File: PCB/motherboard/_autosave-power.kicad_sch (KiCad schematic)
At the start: 28 parts, among them U1 TPS54140ADGQR, U2 PTPS259830LNRGER, U3 AP2112K-3.3TRG1

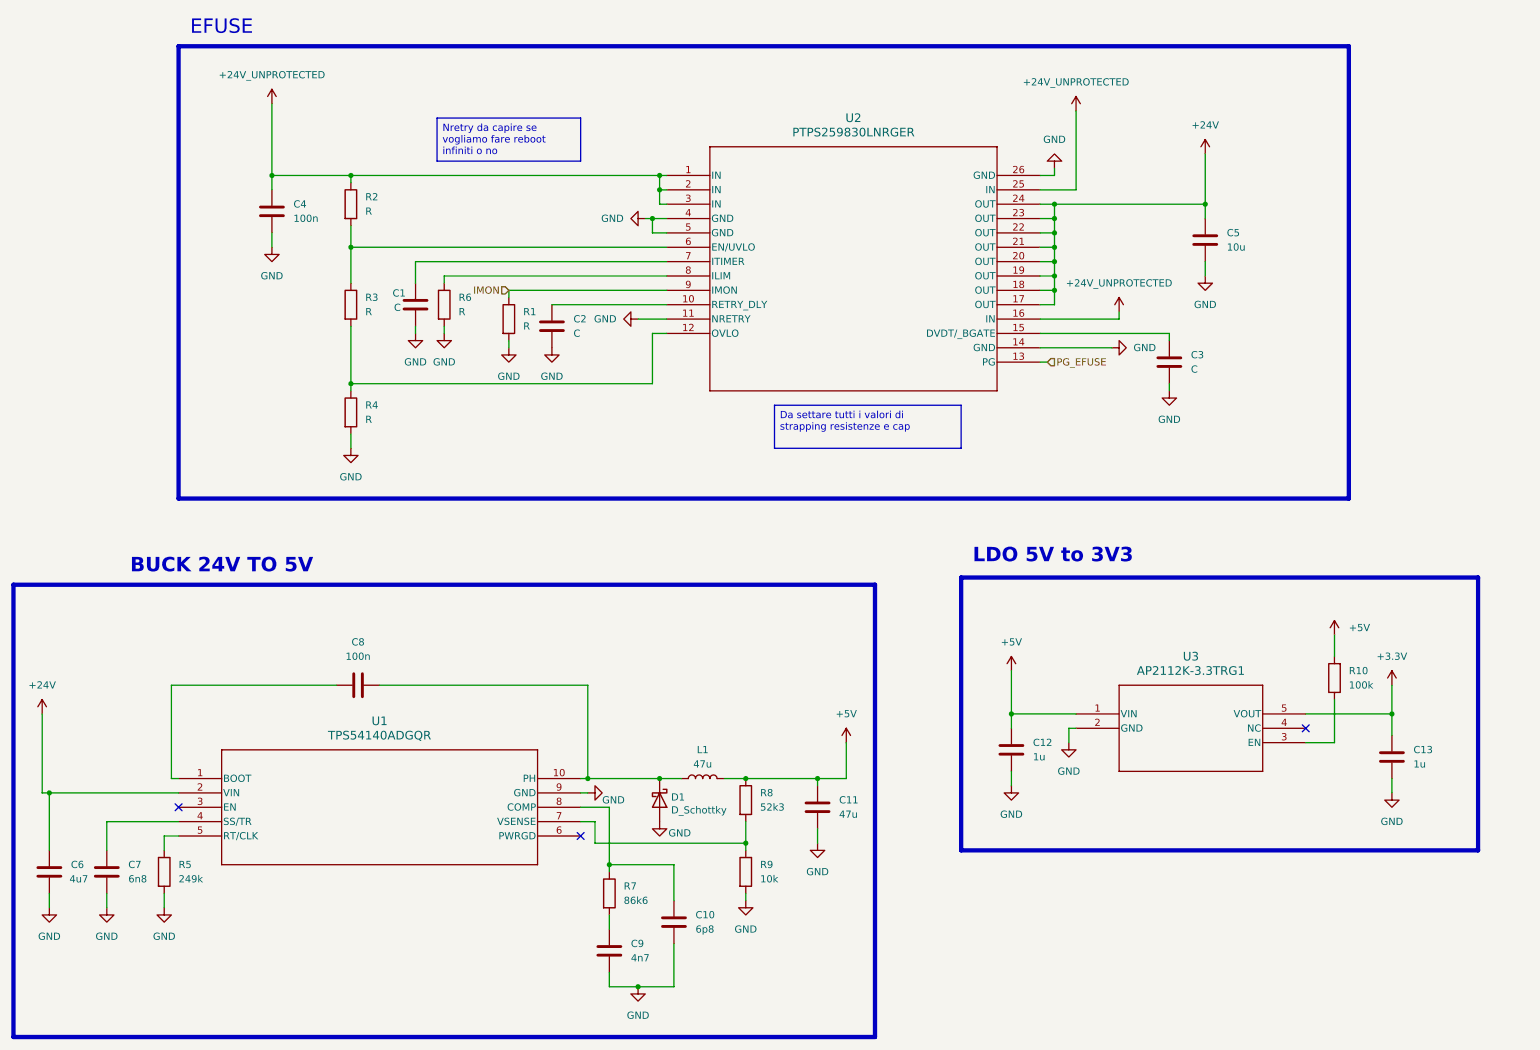
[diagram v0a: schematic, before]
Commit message: aggiunto driver escon in libreria e nel progetto schematico
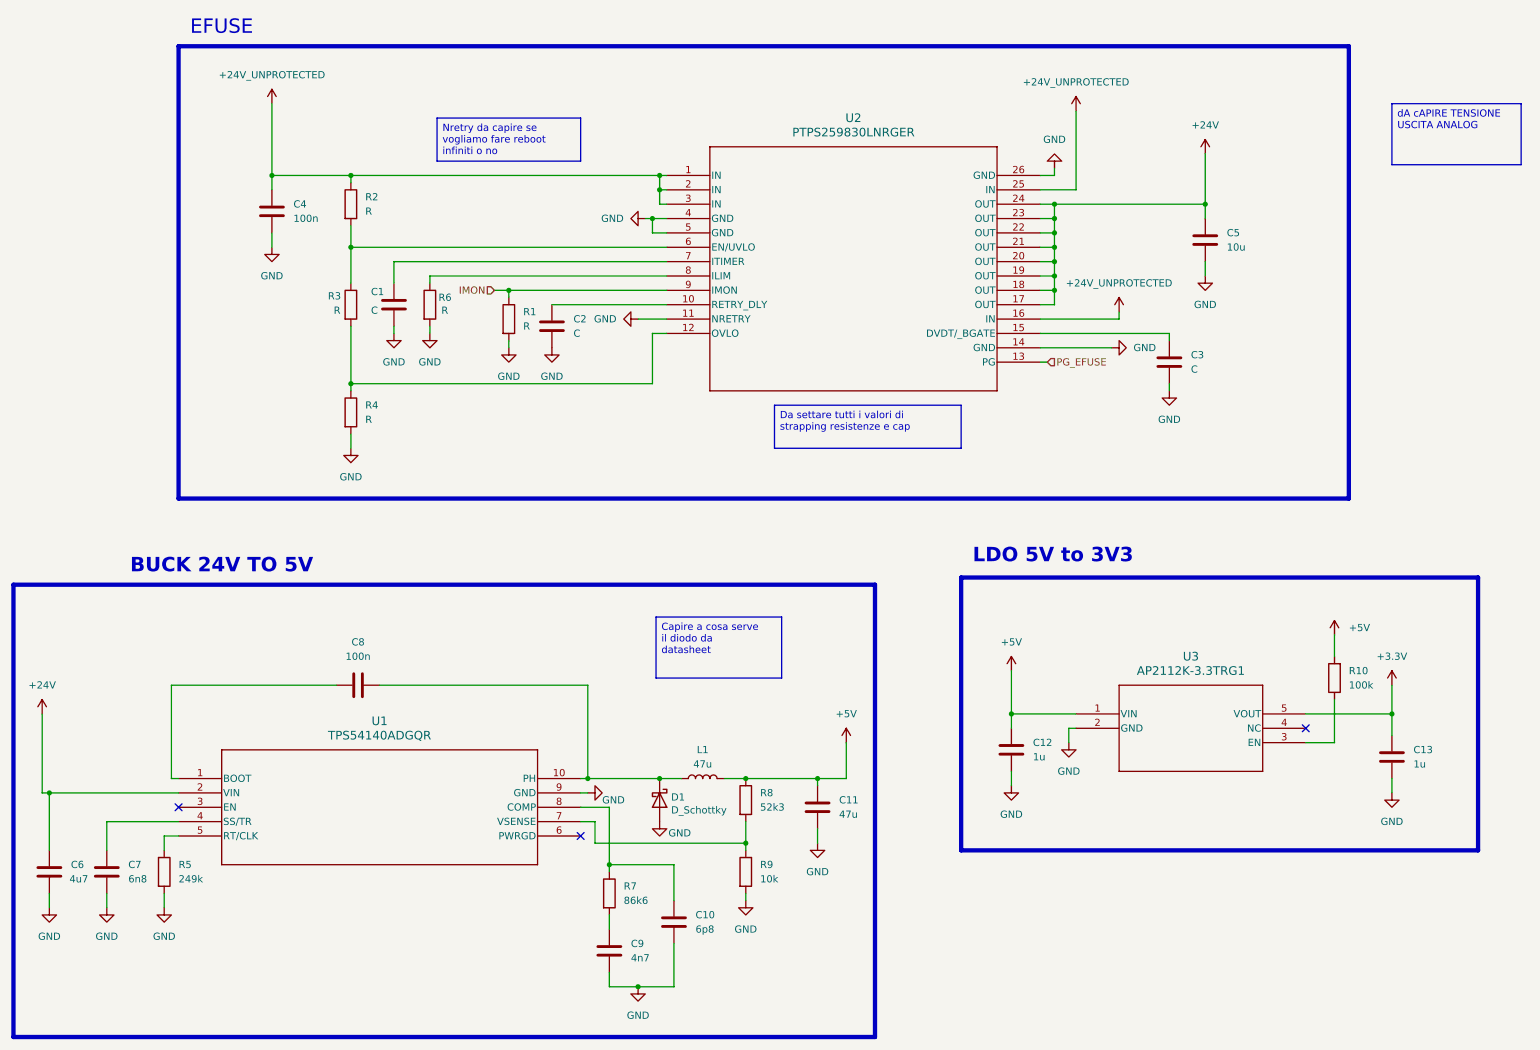
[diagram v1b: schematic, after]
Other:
- moved on the sheet: C1, R6
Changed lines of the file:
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@@
 		)
 	)
+	(text_box "dA cAPIRE TENSIONE USCITA ANALOG \n"
+		(exclude_from_sim no)
+		(at 260.35 27.94 0)
+		(size 22.86 10.795)
+		(margins 0.9525 0.9525 0.9525 0.9525)
+		(stroke
+			(width 0)
+			(type solid)
+		)
+		(fill
+			(type none)
+		)
+		(effects
+			(font
+				(size 1.27 1.27)
+			)
+			(justify left top)
+		)
+	)
 	(text_box "Da settare tutti i valori di strapping resistenze e cap\n"
 		(exclude_from_sim no)
@@
 		)
 	)
+	(text_box "Capire a cosa serve il diodo da datasheet"
+		(exclude_from_sim no)
+		(at 130.175 118.745 0)
+		(size 22.225 10.795)
+		(margins 0.9525 0.9525 0.9525 0.9525)
+		(stroke
+			(width 0)
+			(type solid)
+		)
+		(fill
+			(type none)
+		)
+		(effects
+			(font
+				(size 1.27 1.27)
+			)
+			(justify left top)
+		)
+	)
 	(junction
 		(at 130.81 147.32)
@@
 	)
 	(junction
+		(at 104.14 60.96)
+		(diameter 0)
+		(color 0 0 0 0)
+	)
+	(junction
 		(at 22.86 149.86)
 		(diameter 0)
@@
 	(wire
 		(pts
+			(xy 104.14 60.96) (xy 104.14 62.23)
+		)
+		(stroke
+			(width 0)
+			(type default)
+		)
+	)
+	(wire
+		(pts
 			(xy 62.23 27.94) (xy 62.23 40.64)
 		)
@@
 	(wire
 		(pts
-			(xy 104.14 60.96) (xy 132.08 60.96)
+			(xy 101.6 60.96) (xy 104.14 60.96)
 		)
 		(stroke
@@
 	(wire
 		(pts
-			(xy 87.63 55.88) (xy 132.08 55.88)
+			(xy 83.82 55.88) (xy 132.08 55.88)
 		)
 		(stroke
@@
 	(wire
 		(pts
-			(xy 92.71 58.42) (xy 132.08 58.42)
+			(xy 90.17 58.42) (xy 132.08 58.42)
 		)
 		(stroke
@@
 	(wire
 		(pts
-			(xy 104.14 62.23) (xy 104.14 60.96)
-		)
-		(stroke
-			(width 0)
-			(type default)
-		)
-	)
-	(wire
-		(pts
 			(xy 44.45 130.81) (xy 44.45 147.32)
 		)
@@
 	(wire
 		(pts
-			(xy 92.71 67.31) (xy 92.71 68.58)
+			(xy 90.17 67.31) (xy 90.17 68.58)
 		)
 		(stroke
@@
 	(wire
 		(pts
+			(xy 104.14 60.96) (xy 132.08 60.96)
+		)
+		(stroke
+			(width 0)
+			(type default)
+		)
+	)
+	(wire
+		(pts
 			(xy 43.18 157.48) (xy 45.72 157.48)
 		)
@@
 	(wire
 		(pts
-			(xy 87.63 67.31) (xy 87.63 68.58)
+			(xy 83.82 67.31) (xy 83.82 68.58)
 		)
 		(stroke
@@
 	(wire
 		(pts
-			(xy 92.71 59.69) (xy 92.71 58.42)
+			(xy 90.17 59.69) (xy 90.17 58.42)
 		)
 		(stroke
@@
 	(wire
 		(pts
-			(xy 87.63 59.69) (xy 87.63 55.88)
+			(xy 83.82 59.69) (xy 83.82 55.88)
 		)
 		(stroke
@@
 	(hierarchical_label "IMON"
 		(shape input)
-		(at 104.14 60.96 180)
+		(at 101.6 60.96 180)
 		(effects
 			(font
@@
 	(symbol
 		(lib_id "power:GND")
-		(at 92.71 68.58 0)
+		(at 90.17 68.58 0)
 		(unit 1)
 		(exclude_from_sim no)
@@
 		(fields_autoplaced yes)
 		(property "Reference" "#PWR017"
-			(at 92.71 74.93 0)
+			(at 90.17 74.93 0)
 			(effects
 				(font
@@
 		)
 		(property "Value" "GND"
-			(at 92.71 73.66 0)
+			(at 90.17 73.66 0)
 			(effects
 				(font
@@
 		)
 		(property "Footprint" ""
-			(at 92.71 68.58 0)
+			(at 90.17 68.58 0)
 			(effects
 				(font
@@
 		)
 		(property "Datasheet" ""
-			(at 92.71 68.58 0)
+			(at 90.17 68.58 0)
 			(effects
 				(font
@@
 		)
 		(property "Description" "Power symbol creates a global label with name \"GND\" , ground"
-			(at 92.71 68.58 0)
+			(at 90.17 68.58 0)
 			(effects
 				(font
@@
 	(symbol
 		(lib_id "power:GND")
-		(at 87.63 68.58 0)
+		(at 83.82 68.58 0)
 		(unit 1)
 		(exclude_from_sim no)
@@
 		(fields_autoplaced yes)
 		(property "Reference" "#PWR09"
-			(at 87.63 74.93 0)
+			(at 83.82 74.93 0)
 			(effects
 				(font
@@
 		)
 		(property "Value" "GND"
-			(at 87.63 73.66 0)
+			(at 83.82 73.66 0)
 			(effects
 				(font
@@
 		)
 		(property "Footprint" ""
-			(at 87.63 68.58 0)
+			(at 83.82 68.58 0)
 			(effects
 				(font
@@
 		)
 		(property "Datasheet" ""
-			(at 87.63 68.58 0)
+			(at 83.82 68.58 0)
 			(effects
 				(font
@@
 		)
 		(property "Description" "Power symbol creates a global label with name \"GND\" , ground"
-			(at 87.63 68.58 0)
+			(at 83.82 68.58 0)
 			(effects
 				(font
@@
 	(symbol
 		(lib_id "Device:C")
-		(at 87.63 63.5 0)
+		(at 83.82 63.5 0)
 		(unit 1)
 		(exclude_from_sim no)
@@
 		(dnp no)
 		(property "Reference" "C1"
-			(at 83.566 61.468 0)
+			(at 79.756 61.214 0)
 			(effects
 				(font
@@
 		)
 		(property "Value" "C"
-			(at 83.82 64.008 0)
+			(at 79.756 64.516 0)
 			(effects
 				(font
@@
 		)
 		(property "Footprint" ""
-			(at 88.5952 67.31 0)
+			(at 84.7852 67.31 0)
 			(effects
 				(font
@@
 		)
 		(property "Datasheet" "~"
-			(at 87.63 63.5 0)
+			(at 83.82 63.5 0)
 			(effects
 				(font
@@
 		)
 		(property "Description" "Unpolarized capacitor"
-			(at 87.63 63.5 0)
+			(at 83.82 63.5 0)
 			(effects
 				(font
@@
 	(symbol
 		(lib_id "Device:R")
-		(at 92.71 63.5 0)
+		(at 90.17 63.5 0)
 		(unit 1)
 		(exclude_from_sim no)
@@
 		(on_board yes)
 		(dnp no)
-		(fields_autoplaced yes)
 		(property "Reference" "R6"
-			(at 95.25 62.2299 0)
+			(at 91.694 62.23 0)
 			(effects
 				(font
@@
 		)
 		(property "Value" "R"
-			(at 95.25 64.7699 0)
+			(at 92.202 64.516 0)
 			(effects
 				(font
@@
 		)
 		(property "Footprint" ""
-			(at 90.932 63.5 90)
+			(at 88.392 63.5 90)
 			(effects
 				(font
@@
 		)
 		(property "Datasheet" "~"
-			(at 92.71 63.5 0)
+			(at 90.17 63.5 0)
 			(effects
 				(font
@@
 		)
 		(property "Description" "Resistor"
-			(at 92.71 63.5 0)
+			(at 90.17 63.5 0)
 			(effects
 				(font
@@
 		(on_board yes)
 		(dnp no)
-		(fields_autoplaced yes)
 		(property "Reference" "R3"
-			(at 78.74 62.2299 0)
+			(at 72.136 61.976 0)
 			(effects
 				(font
@@
 		)
 		(property "Value" "R"
-			(at 78.74 64.7699 0)
+			(at 73.152 64.516 0)
 			(effects
 				(font
